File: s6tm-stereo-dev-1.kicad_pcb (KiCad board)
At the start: 4 copper layers, 85 x 80 mm, 190 parts, among them J1 Micro_SD_Card_Det1, J2 Conn_01x04_Pin, J3 USB_C_Receptacle_USB2.0_14P, J4 Conn_01x02, J5 AudioJack4, J6 Conn_01x02, J7 Conn_01x02, J8 Conn_01x02, Q1 Q_NMOS, Q2 Q_NMOS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

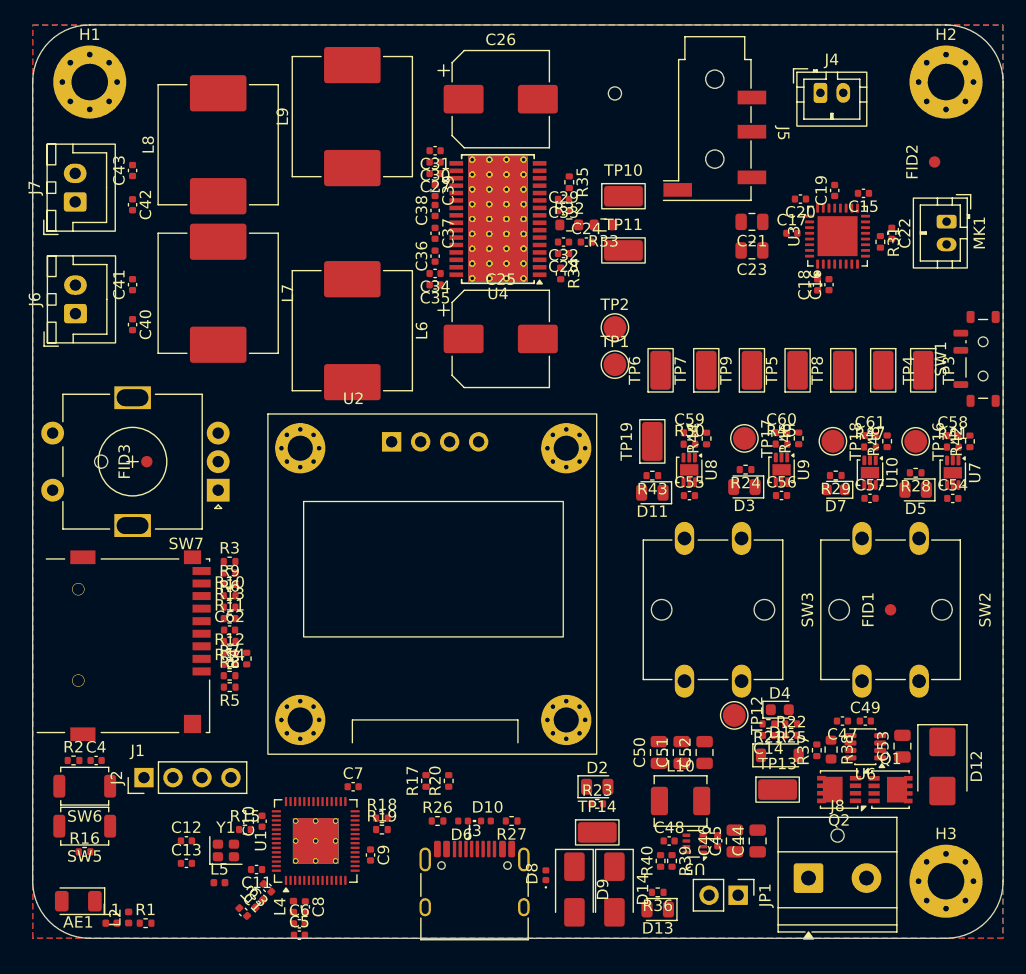
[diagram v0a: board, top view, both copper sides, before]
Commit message: pcb: add gnd vias
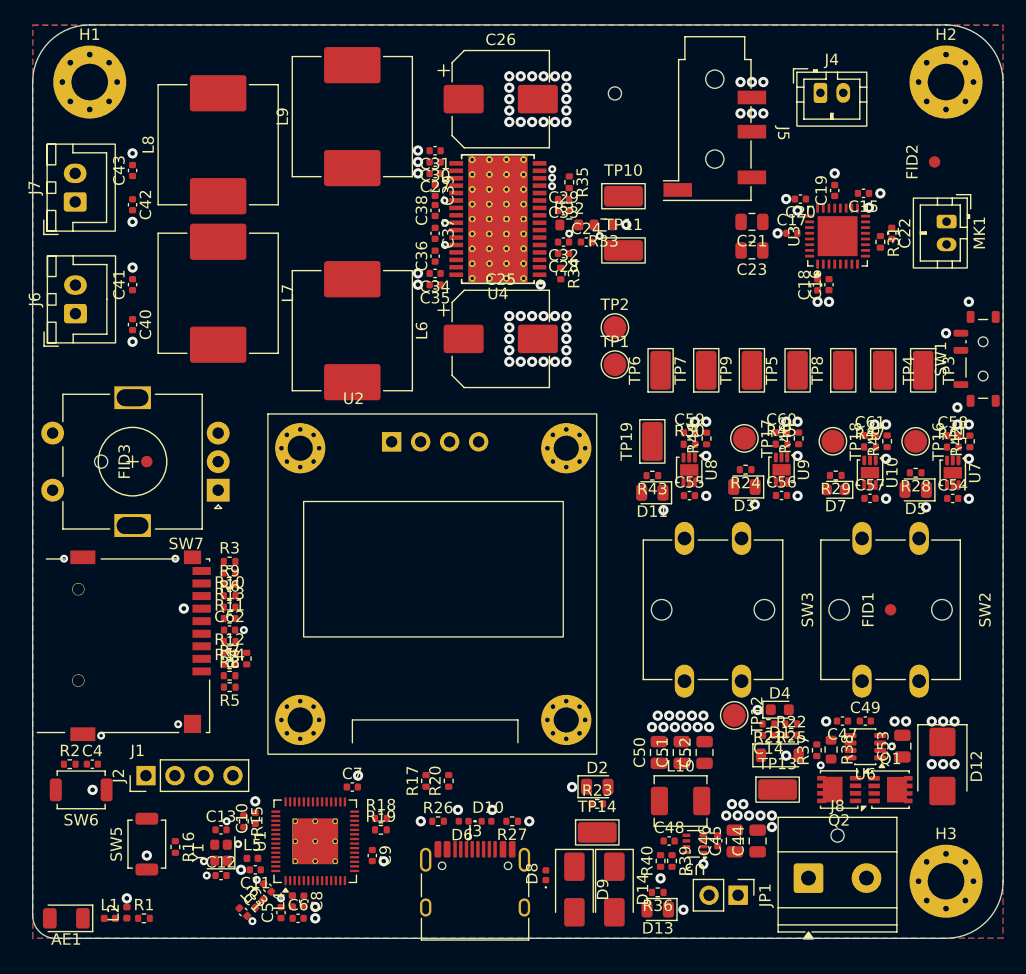
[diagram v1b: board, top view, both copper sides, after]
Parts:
- moved R16 7.96 mm to (129.5, 139.0), turned to -90 degrees
- moved SW5 5.66 mm to (127.0, 138.8), turned to 90 degrees
- moved C12 4.29 mm to (133.5, 141.5)
- moved C13 4.22 mm to (133.5, 137.5)
- moved L5 3.59 mm to (136.2, 140.0)
- moved C5 2.55 mm to (138.8, 144.8), turned to 90 degrees
- moved AE1 1.83 mm to (120.0, 145.2)
- moved R15 0.73 mm to (135.5, 136.8), turned to -90 degrees
- moved C10 0.64 mm to (136.5, 136.5)
- moved C8 0.51 mm to (140.8, 143.8)
- moved C6 0.49 mm to (140.2, 145.2)
- moved L4 0.48 mm to (139.8, 143.8)
- moved Y1 0.47 mm to (133.5, 139.5), turned to 90 degrees
- moved C4 0.46 mm to (122.2, 131.8)
- moved R2 0.46 mm to (120.2, 131.8)
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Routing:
- net GND: vias 0 -> 153
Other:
- outline, holes or cut-outs redrawn

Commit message: pcb: add grid/place origin
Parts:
- moved U2 26.6 mm to (156.8, 128.8), turned to 180 degrees
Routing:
- net GND: vias 153 -> 155

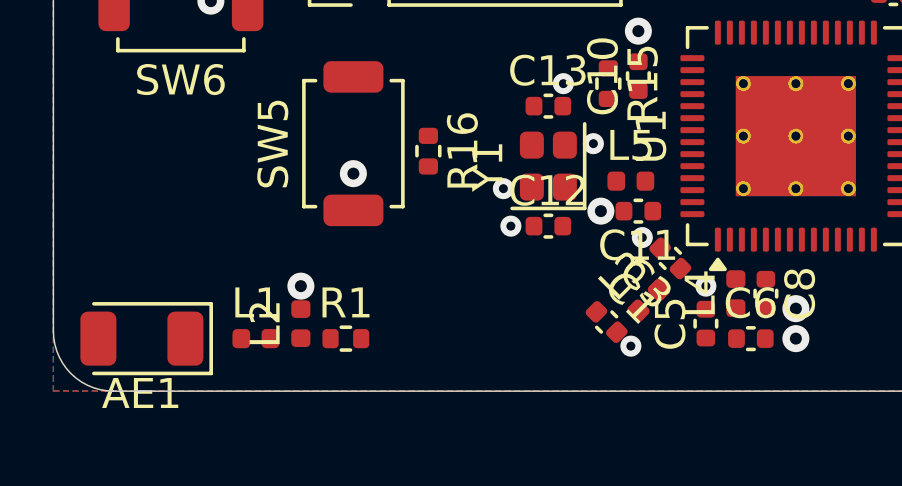
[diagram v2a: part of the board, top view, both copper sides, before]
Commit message: pcb: add rf routing
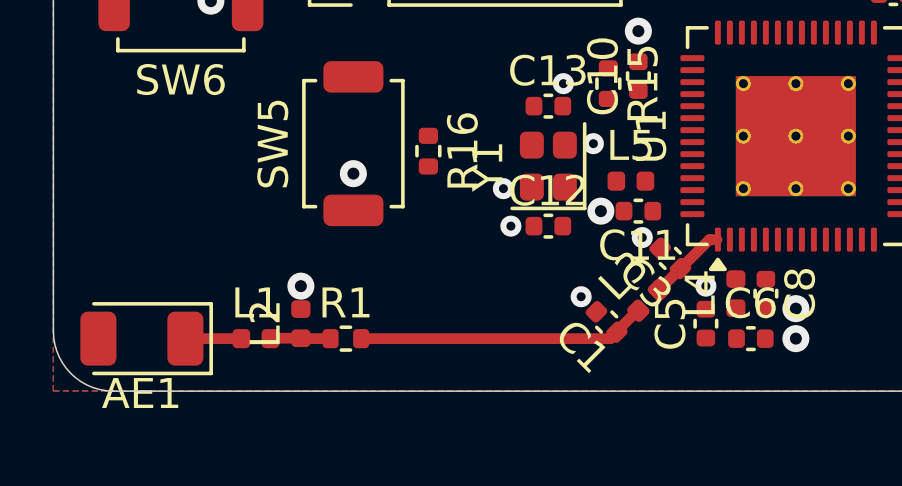
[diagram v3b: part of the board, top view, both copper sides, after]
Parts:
- turned C1 to 135 degrees
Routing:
- net /RF_TRANS: track 0.00 -> 9.65 mm
- net /RF_ESP: track 0.00 -> 2.63 mm
- net Net-(L1-Pad2): track 0.00 -> 2.02 mm
- net /RF_ANT: track 0.00 -> 1.86 mm
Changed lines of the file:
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@@
 	(footprint "Capacitor_SMD:C_0402_1005Metric"
 		(layer "F.Cu")
-		(at 135.442429 144.696249 -45)
+		(at 135.442429 144.696249 135)
 		(descr "Capacitor SMD 0402 (1005 Metric), square (rectangular) end terminal, IPC-7351 nominal, (Body size source: IPC-SM-782 page 76, https://www.pcb-3d.com/wordpress/wp-content/uploads/ipc-sm-782a_amendment_1_and_2.pdf)")
 		(tags "capacitor")
@@
 		)
 		(property "Manufacturer" "Murata"
-			(at 0 0 315)
+			(at 0 0 135)
 			(unlocked yes)
 			(layer "F.Fab")
@@
 		)
 		(property "Manufacturer Part Number" "GJM1555C1H1R2WB01D"
-			(at 0 0 315)
+			(at 0 0 135)
 			(unlocked yes)
 			(layer "F.Fab")
@@
 		)
 		(property "Basic" "X"
-			(at 0 0 315)
+			(at 0 0 135)
 			(unlocked yes)
 			(layer "F.Fab")
@@
 		)
 		(property "JLCPCB Part #" "C76899"
-			(at 0 0 315)
+			(at 0 0 135)
 			(unlocked yes)
 			(layer "F.Fab")
@@
 		(duplicate_pad_numbers_are_jumpers no)
 		(fp_line
-			(start -0.107836 0.36)
-			(end 0.107836 0.36)
+			(start -0.107836 -0.36)
+			(end 0.107836 -0.36)
 			(stroke
 				(width 0.12)
@@
 		)
 		(fp_line
-			(start -0.107836 -0.36)
-			(end 0.107836 -0.36)
+			(start -0.107836 0.36)
+			(end 0.107836 0.36)
 			(stroke
 				(width 0.12)
@@
 		)
 		(pad "1" smd roundrect
-			(at -0.48 0 315)
+			(at -0.48 0 135)
 			(size 0.56 0.62)
 			(layers "F.Cu" "F.Mask" "F.Paste")
@@
 		)
 		(pad "2" smd roundrect
-			(at 0.48 0 315)
+			(at 0.48 0 135)
 			(size 0.56 0.62)
 			(layers "F.Cu" "F.Mask" "F.Paste")
@@
 	)
 	(via
-		(at 136.25 145.5)
+		(at 134.592038 143.85253)
 		(size 0.7)
 		(drill 0.3)
@@
 		(net "GND")
 	)
+	(segment
+		(start 124.25 145.235)
+		(end 124.235 145.25)
+		(width 0.359)
+		(layer "F.Cu")
+		(net "Net-(L1-Pad2)")
+	)
+	(segment
+		(start 125.25 145.235)
+		(end 124.25 145.235)
+		(width 0.359)
+		(layer "F.Cu")
+		(net "Net-(L1-Pad2)")
+	)
+	(segment
+		(start 125.265 145.25)
+		(end 125.25 145.235)
+		(width 0.359)
+		(layer "F.Cu")
+		(net "Net-(L1-Pad2)")
+	)
+	(segment
+		(start 126.24 145.25)
+		(end 125.265 145.25)
+		(width 0.359)
+		(layer "F.Cu")
+		(net "Net-(L1-Pad2)")
+	)
+	(segment
+		(start 135.5675 145.25)
+		(end 127.26 145.25)
+		(width 0.359)
+		(layer "F.Cu")
+		(net "/RF_TRANS")
+	)
+	(segment
+		(start 135.78184 145.03566)
+		(end 135.5675 145.25)
+		(width 0.359)
+		(layer "F.Cu")
+		(net "/RF_TRANS")
+	)
+	(segment
+		(start 136.471094 144.317947)
+		(end 135.76761 145.021431)
+		(width 0.359)
+		(layer "F.Cu")
+		(net "/RF_TRANS")
+	)
+	(segment
+		(start 135.78184 145.03566)
+		(end 135.76761 145.021431)
+		(width 0.359)
+		(layer "F.Cu")
+		(net "/RF_TRANS")
+	)
+	(segment
+		(start 136.499553 144.317947)
+		(end 136.471094 144.317947)
+		(width 0.359)
+		(layer "F.Cu")
+		(net "/RF_TRANS")
+	)
+	(segment
+		(start 137.90316 142.91434)
+		(end 137.185447 143.632053)
+		(width 0.359)
+		(layer "F.Cu")
+		(net "/RF_ESP")
+	)
+	(segment
+		(start 138.8675 141.95)
+		(end 139.1205 141.95)
+		(width 0.359)
+		(layer "F.Cu")
+		(net "/RF_ESP")
+	)
+	(segment
+		(start 137.90316 142.91434)
+		(end 138.8675 141.95)
+		(width 0.359)
+		(layer "F.Cu")
+		(net "/RF_ESP")
+	)
+	(segment
+		(start 123.265 145.25)
+		(end 121.4 145.25)
+		(width 0.359)
+		(layer "F.Cu")
+		(net "/RF_ANT")
+	)
 	(zone

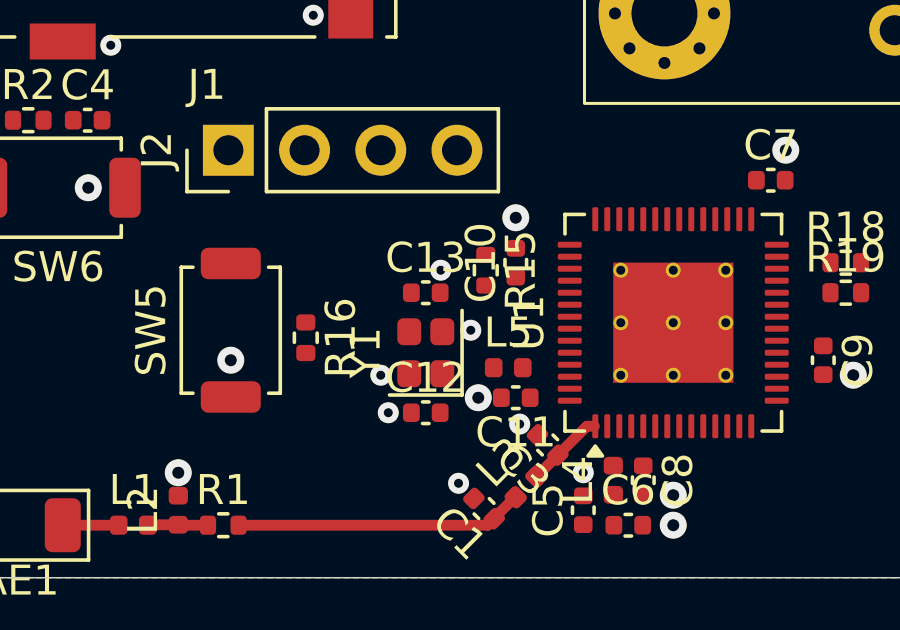
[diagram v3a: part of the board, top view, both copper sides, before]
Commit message: pcb: add HSE xtal routing
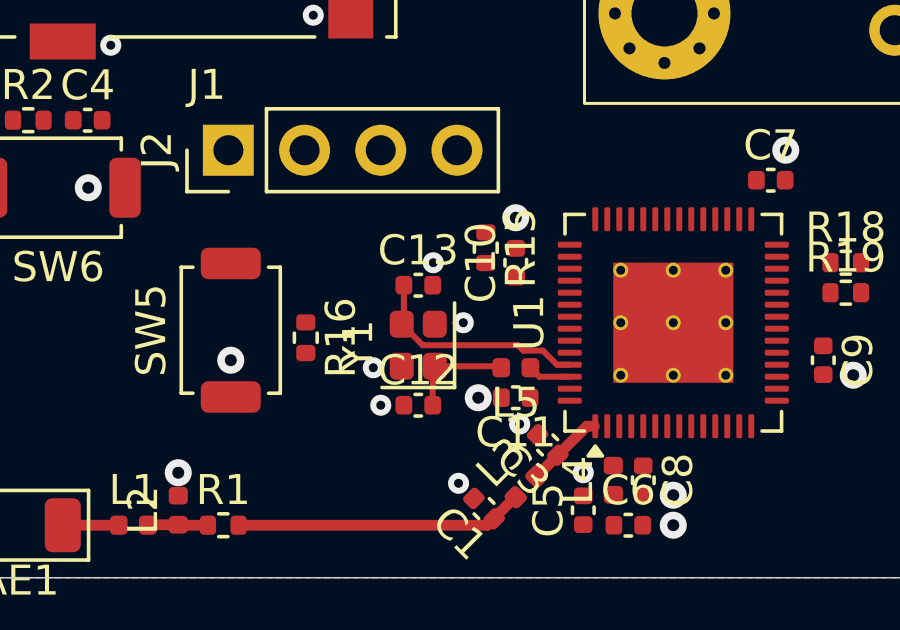
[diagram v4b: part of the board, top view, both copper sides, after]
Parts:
- moved R15 0.75 mm to (135.5, 136.0)
- moved C12 0.35 mm to (133.2, 141.2)
- moved C13 0.35 mm to (133.2, 137.2)
- moved Y1 0.35 mm to (133.2, 139.2)
- moved L5 0.25 mm to (136.5, 140.0), turned to 180 degrees
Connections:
- U1 pad 43: unconnected-(U1-GPIO38-Pad43) -> /ENC_B
- U1 pad 47: /ENC_B -> unconnected-(U1-MTDI/JTAG/GPIO41-Pad47)
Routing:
- net /XTAL_N: track 0.00 -> 7.49 mm
- net /XTAL_PL: track 0.00 -> 3.56 mm
- net /XTAL_P: track 0.00 -> 1.44 mm
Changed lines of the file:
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@@
 	(footprint "Crystal:Crystal_SMD_2016-4Pin_2.0x1.6mm"
 		(layer "F.Cu")
-		(at 133.5 139.5 90)
+		(at 133.25 139.25 90)
 		(descr "SMD2016/4, Crystal, 2.0x1.6mm package, SMD, http://www.q-crystal.com/upload/5/2015552223166229.pdf")
 		(property "Reference" "Y1"
@@
 			(layers "F.Cu" "F.Mask" "F.Paste")
 			(roundrect_rratio 0.25)
-			(net "unconnected-(U1-GPIO38-Pad43)")
+			(net "/ENC_B")
 			(pinfunction "GPIO38_43")
-			(pintype "bidirectional+no_connect")
+			(pintype "bidirectional")
 		)
 		(pad "44" smd roundrect
@@
 			(layers "F.Cu" "F.Mask" "F.Paste")
 			(roundrect_rratio 0.25)
-			(net "/ENC_B")
+			(net "unconnected-(U1-MTDI{slash}JTAG{slash}GPIO41-Pad47)")
 			(pinfunction "MTDI/JTAG/GPIO41_47")
-			(pintype "bidirectional")
+			(pintype "bidirectional+no_connect")
 		)
 		(pad "48" smd roundrect
@@
 	(footprint "Capacitor_SMD:C_0402_1005Metric"
 		(layer "F.Cu")
-		(at 133.5 137.5)
+		(at 133.25 137.25)
 		(descr "Capacitor SMD 0402 (1005 Metric), square (rectangular) end terminal, IPC-7351 nominal, (Body size source: IPC-SM-782 page 76, https://www.pcb-3d.com/wordpress/wp-content/uploads/ipc-sm-782a_amendment_1_and_2.pdf)")
 		(tags "capacitor")
@@
 	(footprint "Capacitor_SMD:C_0402_1005Metric"
 		(layer "F.Cu")
-		(at 133.5 141.5)
+		(at 133.25 141.25)
 		(descr "Capacitor SMD 0402 (1005 Metric), square (rectangular) end terminal, IPC-7351 nominal, (Body size source: IPC-SM-782 page 76, https://www.pcb-3d.com/wordpress/wp-content/uploads/ipc-sm-782a_amendment_1_and_2.pdf)")
 		(tags "capacitor")
@@
 	(footprint "Inductor_SMD:L_0402_1005Metric"
 		(layer "F.Cu")
-		(at 136.25 140)
+		(at 136.5 140 180)
 		(descr "Inductor SMD 0402 (1005 Metric), square (rectangular) end terminal, IPC-7351 nominal, (Body size source: http://www.tortai-tech.com/upload/download/2011102023233369053.pdf)")
 		(tags "inductor")
@@
 		)
 		(property "Manufacturer" "Murata"
-			(at 0 0 0)
+			(at 0 0 180)
 			(unlocked yes)
 			(layer "F.Fab")
@@
 		)
 		(property "Manufacturer Part Number" "LQW15AN24NG00D"
-			(at 0 0 0)
+			(at 0 0 180)
 			(unlocked yes)
 			(layer "F.Fab")
@@
 		)
 		(property "Basic" "X"
-			(at 0 0 0)
+			(at 0 0 180)
 			(unlocked yes)
 			(layer "F.Fab")
@@
 		)
 		(property "JLCPCB Part #" "C167472"
-			(at 0 0 0)
+			(at 0 0 180)
 			(unlocked yes)
 			(layer "F.Fab")
@@
 		)
 		(pad "1" smd roundrect
-			(at -0.485 0)
+			(at -0.485 0 180)
 			(size 0.59 0.64)
 			(layers "F.Cu" "F.Mask" "F.Paste")
@@
 		)
 		(pad "2" smd roundrect
-			(at 0.485 0)
+			(at 0.485 0 180)
 			(size 0.59 0.64)
 			(layers "F.Cu" "F.Mask" "F.Paste")
@@
 	(footprint "Resistor_SMD:R_0402_1005Metric"
 		(layer "F.Cu")
-		(at 135.5 136.75 -90)
+		(at 135.5 136 -90)
 		(descr "Resistor SMD 0402 (1005 Metric), square (rectangular) end terminal, IPC-7351 nominal, (Body size source: IPC-SM-782 page 72, https://www.pcb-3d.com/wordpress/wp-content/uploads/ipc-sm-782a_amendment_1_and_2.pdf)")
 		(tags "resistor")
@@
 	)
 	(via
-		(at 132 140.25)
+		(at 131.75 140)
 		(size 0.7)
 		(drill 0.3)
@@
 	)
 	(via
-		(at 132.25 141.5)
+		(at 132 141.25)
 		(size 0.7)
 		(drill 0.3)
@@
 	)
 	(via
-		(at 134 136.75)
+		(at 133.75 136.5)
 		(size 0.7)
 		(drill 0.3)
@@
 	)
 	(via
-		(at 135 138.75)
+		(at 134.75 138.5)
 		(size 0.7)
 		(drill 0.3)
@@
 	)
 	(segment
+		(start 133.73 141.25)
+		(end 133.73 140.02)
+		(width 0.2)
+		(layer "F.Cu")
+		(net "/XTAL_PL")
+	)
+	(segment
+		(start 135.965 139.95)
+		(end 136.015 140)
+		(width 0.2)
+		(layer "F.Cu")
+		(net "/XTAL_PL")
+	)
+	(segment
+		(start 133.73 140.02)
+		(end 133.8 139.95)
+		(width 0.2)
+		(layer "F.Cu")
+		(net "/XTAL_PL")
+	)
+	(segment
+		(start 133.8 139.95)
+		(end 135.965 139.95)
+		(width 0.2)
+		(layer "F.Cu")
+		(net "/XTAL_PL")
+	)
+	(segment
+		(start 137.87435 139.9)
+		(end 137.40435 139.43)
+		(width 0.2)
+		(layer "F.Cu")
+		(net "/XTAL_N")
+	)
+	(segment
+		(start 136.57 139.25)
+		(end 133.4 139.25)
+		(width 0.2)
+		(layer "F.Cu")
+		(net "/XTAL_N")
+	)
+	(segment
+		(start 132.77 138.48)
+		(end 132.7 138.55)
+		(width 0.2)
+		(layer "F.Cu")
+		(net "/XTAL_N")
+	)
+	(segment
+		(start 137.40435 139.43)
+		(end 136.75 139.43)
+		(width 0.2)
+		(layer "F.Cu")
+		(net "/XTAL_N")
+	)
+	(segment
+		(start 133.4 139.25)
+		(end 132.7 138.55)
+		(width 0.2)
+		(layer "F.Cu")
+		(net "/XTAL_N")
+	)
+	(segment
+		(start 136.75 139.43)
+		(end 136.57 139.25)
+		(width 0.2)
+		(layer "F.Cu")
+		(net "/XTAL_N")
+	)
+	(segment
+		(start 132.77 137.25)
+		(end 132.77 138.48)
+		(width 0.2)
+		(layer "F.Cu")
+		(net "/XTAL_N")
+	)
+	(segment
+		(start 138.3 139.9)
+		(end 137.87435 139.9)
+		(width 0.2)
+		(layer "F.Cu")
+		(net "/XTAL_N")
+	)
+	(segment
 		(start 137.90316 142.91434)
 		(end 137.185447 143.632053)
@@
 	)
 	(segment
+		(start 137.285 140.3)
+		(end 136.985 140)
+		(width 0.2)
+		(layer "F.Cu")
+		(net "/XTAL_P")
+	)
+	(segment
+		(start 138.3 140.3)
+		(end 137.285 140.3)
+		(width 0.2)
+		(layer "F.Cu")
+		(net "/XTAL_P")
+	)
+	(segment
 		(start 123.265 145.25)
 		(end 121.4 145.25)
@@
 	)
 	(zone
+		(layer "F.Cu")
+		(hatch edge 0.5)
+		(connect_pads
+			(clearance 0)
+		)
+		(min_thickness 0.25)
+		(keepout
+			(tracks allowed)
+			(vias allowed)
+			(pads allowed)
+			(copperpour not_allowed)
+			(footprints allowed)
+		)
+		(placement
+			(enabled no)
+			(sheetname "/")
+		)
+		(fill
+			(thermal_gap 0.5)
+			(thermal_bridge_width 0.5)
+			(island_removal_mode 0)
+		)
+		(polygon
+			(pts
+				(xy 132.25 141.5) (xy 131.75 141) (xy 131.75 137.75) (xy 132.25 137.25) (xy 134.25 137.25) (xy 135.25 138.25)
+				(xy 135.25 141) (xy 134.75 141.5)
+			)
+		)
+	)
+	(zone
